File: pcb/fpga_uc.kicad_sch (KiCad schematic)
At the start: 13 parts, among them J1401 FPGA_JTAG, U1402 S25FL127SABMFV101, U666 XC7A75T-FTG256

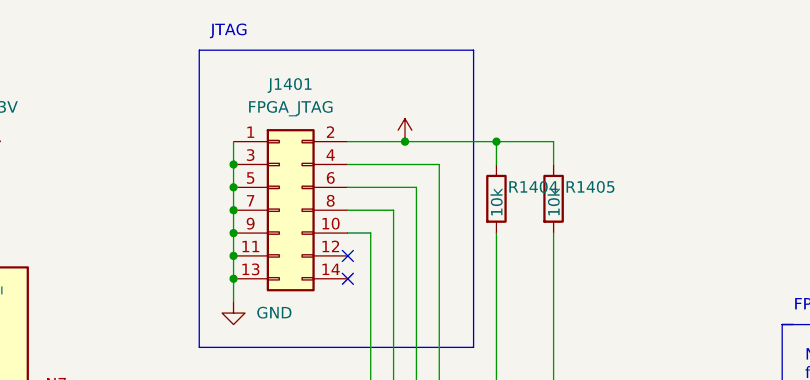
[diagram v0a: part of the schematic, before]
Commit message: switch some pins for more erqonomiq layout
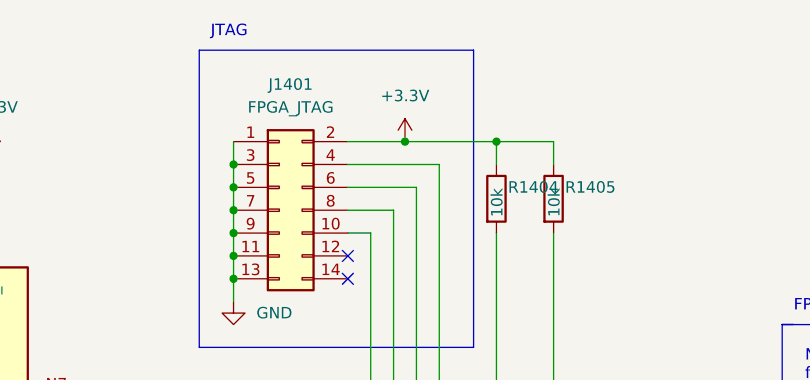
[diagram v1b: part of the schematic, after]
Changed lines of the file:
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@@
       (effects (font (size 1.27 1.27)) hide)
     )
-    (property "Value" "" (id 1) (at 140.97 50.8 0))
+    (property "Value" "+3.3V" (id 1) (at 140.97 50.8 0))
     (property "Footprint" "" (id 2) (at 140.97 55.88 0)
       (effects (font (size 1.27 1.27)) hide)

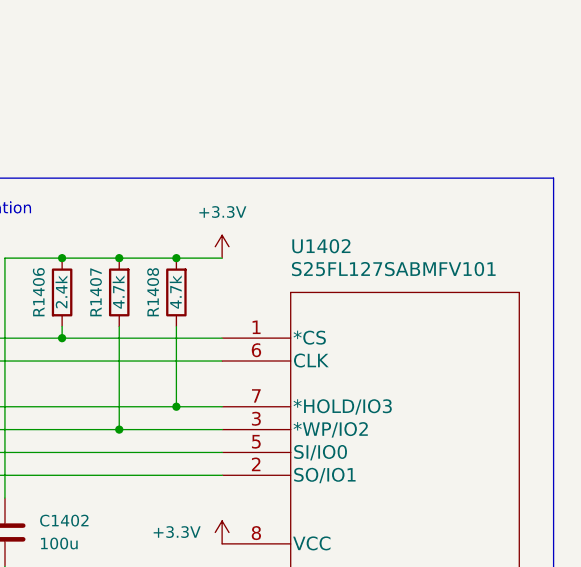
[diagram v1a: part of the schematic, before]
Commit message: assign the last footprints
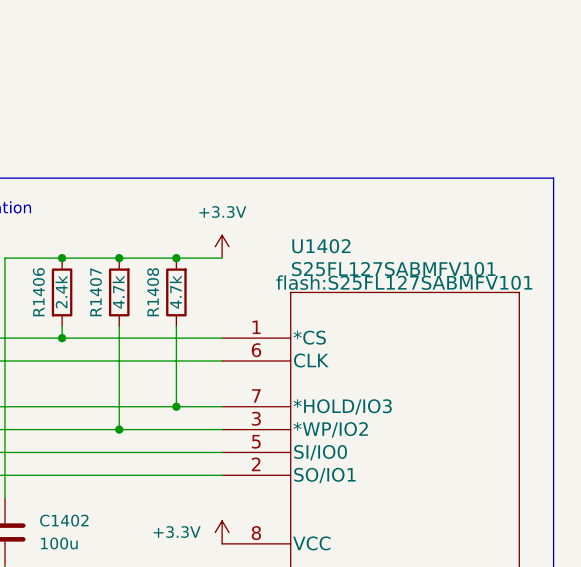
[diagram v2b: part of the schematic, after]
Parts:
- U1402: footprint SOC008_SPA -> flash:S25FL127SABMFV101
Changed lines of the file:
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@@
       (effects (font (size 1.524 1.524)) (justify left))
     )
-    (property "Footprint" "SOC008_SPA" (id 2) (at 256.54 87.884 0)
-      (effects (font (size 1.524 1.524)) hide)
+    (property "Footprint" "flash:S25FL127SABMFV101" (id 2) (at 256.54 87.884 0)
+      (effects (font (size 1.524 1.524)))
     )
     (property "Datasheet" "" (id 3) (at 236.22 93.98 0)

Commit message: is donegst
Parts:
- J1401: footprint Connector_PinHeader_2.54mm:PinHeader_2x07_P2.54mm_Vertical_SMD -> Connector_PinHeader_2.54mm:PinHeader_2x07_P2.54mm_Vertical
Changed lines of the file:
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@@
     (property "Reference" "J1401" (id 0) (at 128.27 49.53 0))
     (property "Value" "FPGA_JTAG" (id 1) (at 128.27 52.07 0))
-    (property "Footprint" "Connector_PinHeader_2.54mm:PinHeader_2x07_P2.54mm_Vertical_SMD" (id 2) (at 127 63.5 0)
+    (property "Footprint" "Connector_PinHeader_2.54mm:PinHeader_2x07_P2.54mm_Vertical" (id 2) (at 127 63.5 0)
       (effects (font (size 1.27 1.27)) hide)
     )

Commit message: fix capacitor values and footprints
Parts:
- C1401: footprint Capacitor_SMD:C_0805_2012Metric_Pad1.18x1.45mm_HandSolder -> Capacitor_SMD:C_1210_3225Metric_Pad1.33x2.70mm_HandSolder
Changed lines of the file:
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@@
       (effects (font (size 1.27 1.27)) (justify left))
     )
-    (property "Footprint" "Capacitor_SMD:C_0805_2012Metric_Pad1.18x1.45mm_HandSolder" (id 2) (at 86.0552 64.77 0)
+    (property "Footprint" "Capacitor_SMD:C_1210_3225Metric_Pad1.33x2.70mm_HandSolder" (id 2) (at 86.0552 64.77 0)
       (effects (font (size 1.27 1.27)) hide)
     )
